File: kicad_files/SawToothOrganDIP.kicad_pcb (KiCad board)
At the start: 2 copper layers, 100 x 67.6 mm, 41 parts, among them J1 Conn_01x01, J2 Conn_01x01, J3 Conn_01x01, Q1 Q_NPN_CBE, Q2 Q_NPN_CBE, Q3 Q_NPN_CBE, Q4 Q_PNP_CBE, SW1 SW_DIP_x01, U1 Keyboard

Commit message: added logos to the pcb
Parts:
- added Ref**: Val**, Binary_Kitchen:Kitchen_Logo_10mm, F.Cu at (186.5, 139.5)
- added Ref**: Val**, Binary_Kitchen:Tettnang_Logo, F.Cu at (212.5, 139.0)
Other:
- board text added: "CC-BY-SA 4.0"
- board text added: "Saw Tooth Organ"
- board text added: "emuseum-tettnang.de"
- board text added: "v1.0"

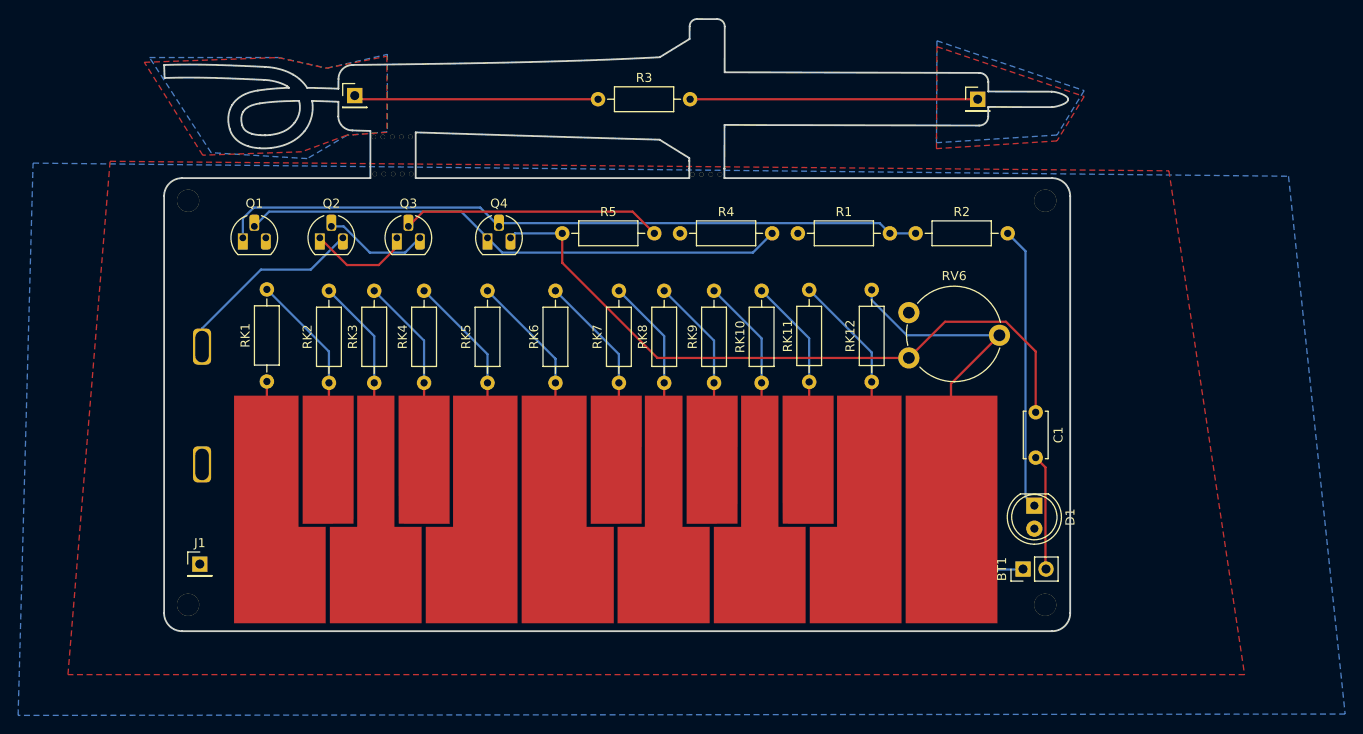
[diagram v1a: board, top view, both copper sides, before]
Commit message: added gerber-files and another resistor
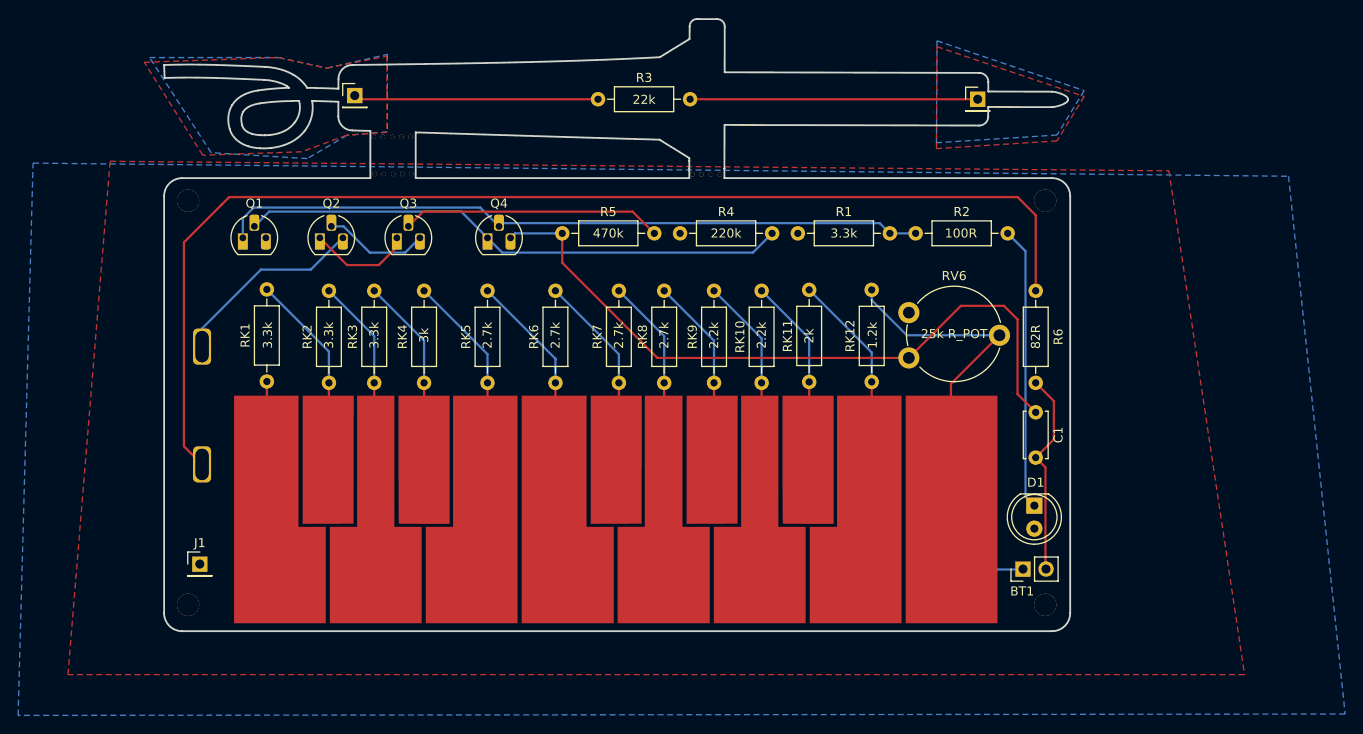
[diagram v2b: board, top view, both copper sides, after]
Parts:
- added R6: 82R, Resistor_THT:R_Axial_DIN0207_L6.3mm_D2.5mm_P10.16mm_Horizontal, F.Cu at (235.5, 131.0)
- R2: value 100 -> 100R
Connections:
- LS1 pad 1: GND -> Net-(LS1-Pad1)
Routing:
- net Net-(LS1-Pad1): track 0.00 -> 130.6 mm
- net GND: track 12.8 -> 22.7 mm
- net Net-(C1-Pad1): track 75.5 -> 77.8 mm

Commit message: adjusted outline to be produceable
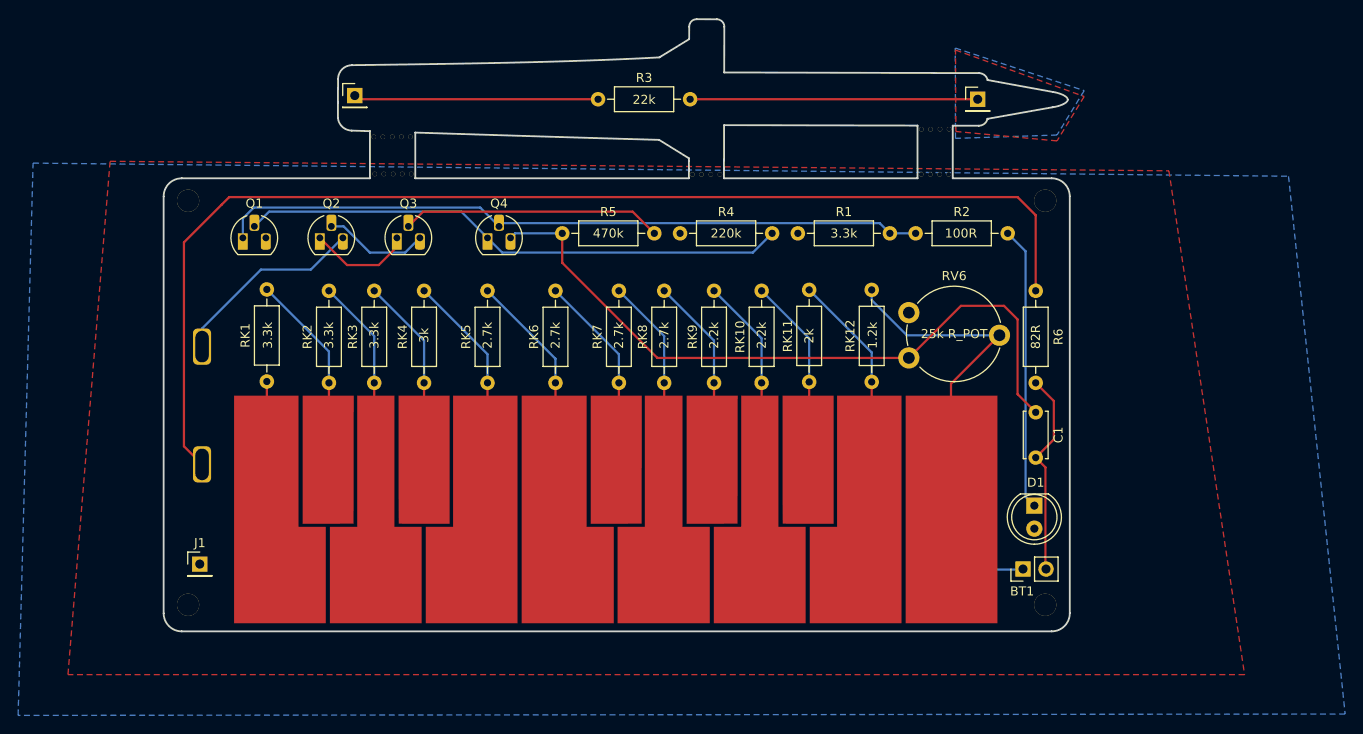
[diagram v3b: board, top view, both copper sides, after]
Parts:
- added Ref**: Val**, Binary_Kitchen:MouseBites, F.Cu at (225.4, 103.0)
- added Ref**: Val**, Binary_Kitchen:MouseBites, F.Cu at (223.4, 103.0)
- added Ref**: Val**, Binary_Kitchen:MouseBites, F.Cu at (225.4, 108.0)
- added Ref**: Val**, Binary_Kitchen:MouseBites, F.Cu at (223.4, 108.0)
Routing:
- removed copper zone on B.Cu, net Net-(J2-Pad1)
- removed copper zone on F.Cu, net Net-(J2-Pad1)
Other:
- outline, holes or cut-outs redrawn

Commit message: added NPN and PNP to transistors
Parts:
- Q1, Q2, Q3: value Q_NPN_CBE -> NPN
- Q4: value Q_PNP_CBE -> PNP

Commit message: some minor fixes for version 1.1
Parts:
- added REF**: MountingHole_2.1mm, MountingHole:MountingHole_2.1mm, F.Cu at (160.9, 99.7)
- added REF**: MountingHole_2.1mm, MountingHole:MountingHole_2.1mm, F.Cu at (143.3, 146.8)
- added REF**: MountingHole_2.1mm, MountingHole:MountingHole_2.1mm, F.Cu at (234.1, 148.8)
- added REF**: MountingHole_2.1mm, MountingHole:MountingHole_2.1mm, F.Cu at (236.7, 148.8)
- moved J2 4.30 mm to (164.6, 99.7)
- moved D1 1.83 mm to (235.4, 142.7)
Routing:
- net Net-(J2-Pad1): track 27.0 -> 22.6 mm
- net Net-(D1-Pad1): track 31.3 -> 29.7 mm
- net GND: track 22.7 -> 24.1 mm
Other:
- board text added: "+"
- board text added: "Stylus"
- board text added: "v1.1"
- board text removed: "v1.0"
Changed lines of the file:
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@@
   (general
     (thickness 1.6)
-    (drawings 60)
-    (tracks 110)
+    (drawings 62)
+    (tracks 112)
     (zones 0)
-    (modules 48)
+    (modules 52)
     (nets 28)
   )
@@
     (mod_text_size 1 1)
     (mod_text_width 0.15)
-    (pad_size 1.524 1.524)
-    (pad_drill 0.762)
+    (pad_size 1.5 1.5)
+    (pad_drill 1.5)
     (pad_to_mask_clearance 0.05)
     (aux_axis_origin 0 0)
@@
     (add_net VS)
   )
+  (module MountingHole:MountingHole_2.1mm (layer F.Cu)
+    (at 160.95 99.72)
+    (descr "Mounting Hole 2.1mm, no annular")
+    (tags "mounting hole 2.1mm no annular")
+    (attr virtual)
+    (fp_text reference REF** (at 0 -3.2) (layer F.SilkS) hide
+      (effects (font (size 1 1) (thickness 0.15)))
+    )
+    (fp_text value MountingHole_2.1mm (at 0 3.2) (layer F.Fab)
+      (effects (font (size 1 1) (thickness 0.15)))
+    )
+    (pad "" np_thru_hole circle (at 0 0) (size 1.5 1.5) (drill 1.5) (layers *.Cu *.Mask))
+  )
+  (module MountingHole:MountingHole_2.1mm (layer F.Cu)
+    (at 143.31 146.77)
+    (descr "Mounting Hole 2.1mm, no annular")
+    (tags "mounting hole 2.1mm no annular")
+    (attr virtual)
+    (fp_text reference REF** (at 0 -3.2) (layer F.SilkS) hide
+      (effects (font (size 1 1) (thickness 0.15)))
+    )
+    (fp_text value MountingHole_2.1mm (at 0 3.2) (layer F.Fab)
+      (effects (font (size 1 1) (thickness 0.15)))
+    )
+    (pad "" np_thru_hole circle (at 0 0) (size 1.5 1.5) (drill 1.5) (layers *.Cu *.Mask))
+  )
+  (module MountingHole:MountingHole_2.1mm (layer F.Cu)
+    (at 234.12 148.78)
+    (descr "Mounting Hole 2.1mm, no annular")
+    (tags "mounting hole 2.1mm no annular")
+    (attr virtual)
+    (fp_text reference REF** (at 0 -3.2) (layer F.SilkS) hide
+      (effects (font (size 1 1) (thickness 0.15)))
+    )
+    (fp_text value MountingHole_2.1mm (at 0 3.2) (layer F.Fab)
+      (effects (font (size 1 1) (thickness 0.15)))
+    )
+    (pad "" np_thru_hole circle (at 0 0) (size 1.5 1.5) (drill 1.5) (layers *.Cu *.Mask))
+  )
+  (module MountingHole:MountingHole_2.1mm (layer F.Cu)
+    (at 236.71 148.79)
+    (descr "Mounting Hole 2.1mm, no annular")
+    (tags "mounting hole 2.1mm no annular")
+    (attr virtual)
+    (fp_text reference REF** (at 0 -3.2) (layer F.SilkS) hide
+      (effects (font (size 1 1) (thickness 0.15)))
+    )
+    (fp_text value MountingHole_2.1mm (at 0 3.2) (layer F.Fab)
+      (effects (font (size 1 1) (thickness 0.15)))
+    )
+    (pad "" np_thru_hole circle (at 0 0) (size 1.5 1.5) (drill 1.5) (layers *.Cu *.Mask))
+  )
   (module SawToothOrganDIP:pad_solder_iron (layer F.Cu)
     (at 189.15 100.5)
@@
   )
   (module Connector_PinHeader_2.54mm:PinHeader_1x01_P2.54mm_Vertical (layer F.Cu)
-    (at 160.35 99.3)
+    (at 164.63 99.68)
     (descr "Through hole straight pin header, 1x01, 2.54mm pitch, single row")
     (tags "Through hole pin header THT 1x01 2.54mm single row")
@@
   )
   (module LED_THT:LED_D5.0mm_Clear (layer F.Cu)
-    (at 235.35 144.55 270)
+    (at 235.39 142.72 270)
     (descr "LED, diameter 5.0mm, 2 pins, http://cdn-reichelt.de/documents/datenblatt/A500/LL-504BC2E-009.pdf")
     (tags "LED diameter 5.0mm 2 pins")
@@
       (rotate (xyz 0 0 0))
     )
+  )
+  (gr_text Stylus (at 143.3 153.15) (layer B.SilkS)
+    (effects (font (size 1 1) (thickness 0.15)) (justify mirror))
+  )
+  (gr_text + (at 234.16 153.53) (layer B.SilkS)
+    (effects (font (size 2 2) (thickness 0.15)) (justify mirror))
   )
   (gr_line (start 167.029194 103.379639) (end 167.029194 103.379639) (layer Edge.Cuts) (width 0.2))
@@
   (gr_line (start 141.26074 158.425897) (end 237.260059 158.425897) (layer Edge.Cuts) (width 0.2))
   (gr_line (start 158.5 100) (end 158.499483 100.107487) (layer Edge.Cuts) (width 0.2))
-  (gr_text "v1.0\n" (at 170 154) (layer B.SilkS)
-    (effects (font (size 0.508 0.508) (thickness 0.127)) (justify mirror))
+  (gr_text "v1.1\n" (at 170 154) (layer B.SilkS)
+    (effects (font (size 0.6 0.6) (thickness 0.127)) (justify mirror))
   )
   (gr_text "CC-BY-SA 4.0" (at 179 154.5) (layer B.SilkS)
@@
   )
   (segment (start 236.575001 151.485001) (end 236.64 151.55) (width 0.25) (layer F.Cu) (net 1))
-  (segment (start 236.575001 140.325001) (end 236.575001 151.485001) (width 0.25) (layer F.Cu) (net 1))
-  (segment (start 235.5 139.25) (end 236.575001 140.325001) (width 0.25) (layer F.Cu) (net 1))
   (segment (start 235.5 139.25) (end 237.5 137.25) (width 0.25) (layer F.Cu) (net 1))
   (segment (start 237.5 133) (end 235.5 131) (width 0.25) (layer F.Cu) (net 1))
   (segment (start 237.5 137.25) (end 237.5 133) (width 0.25) (layer F.Cu) (net 1))
+  (segment (start 236.64 151.55) (end 238.22 149.97) (width 0.25) (layer F.Cu) (net 1))
+  (segment (start 238.22 141.97) (end 235.5 139.25) (width 0.25) (layer F.Cu) (net 1))
+  (segment (start 238.22 149.97) (end 238.22 141.97) (width 0.25) (layer F.Cu) (net 1))
   (segment (start 234.05 151.6) (end 234.1 151.55) (width 0.25) (layer B.Cu) (net 2))
   (segment (start 227.95 151.6) (end 234.05 151.6) (width 0.25) (layer B.Cu) (net 2))
@@
   (segment (start 159.5 118) (end 156.5 115) (width 0.25) (layer F.Cu) (net 4))
   (segment (start 163 118) (end 159.5 118) (width 0.25) (layer F.Cu) (net 4))
-  (segment (start 234.374999 116.464999) (end 232.41 114.5) (width 0.25) (layer B.Cu) (net 5))
-  (segment (start 234.374999 143.574999) (end 234.374999 116.464999) (width 0.25) (layer B.Cu) (net 5))
-  (segment (start 235.35 144.55) (end 234.374999 143.574999) (width 0.25) (layer B.Cu) (net 5))
+  (segment (start 233.209999 115.299999) (end 233.209999 140.929999) (width 0.25) (layer B.Cu) (net 5))
+  (segment (start 232.41 114.5) (end 233.209999 115.299999) (width 0.25) (layer B.Cu) (net 5))
+  (segment (start 235 142.72) (end 235.39 142.72) (width 0.25) (layer B.Cu) (net 5))
+  (segment (start 233.209999 140.929999) (end 235 142.72) (width 0.25) (layer B.Cu) (net 5))
   (segment (start 222.25 114.5) (end 219.41 114.5) (width 0.25) (layer B.Cu) (net 6))
   (segment (start 176.625001 113.374999) (end 176.27 113.73) (width 0.25) (layer B.Cu) (net 6))
@@
   (segment (start 217.4 121.87137) (end 221.27863 125.75) (width 0.25) (layer B.Cu) (net 21))
   (segment (start 217.4 120.74) (end 217.4 121.87137) (width 0.25) (layer B.Cu) (net 21))
-  (segment (start 160.75 99.7) (end 160.35 99.3) (width 0.25) (layer F.Cu) (net 23))
-  (segment (start 187.2 99.7) (end 160.75 99.7) (width 0.25) (layer F.Cu) (net 23))
+  (segment (start 164.65 99.7) (end 164.63 99.68) (width 0.25) (layer F.Cu) (net 23))
+  (segment (start 187.2 99.7) (end 164.65 99.7) (width 0.25) (layer F.Cu) (net 23))
   (segment (start 229.1 99.7) (end 197.36 99.7) (width 0.25) (layer F.Cu) (net 24))
   (segment (start 167.89501 112.10499) (end 166.27 113.73) (width 0.25) (layer F.Cu) (net 25))
